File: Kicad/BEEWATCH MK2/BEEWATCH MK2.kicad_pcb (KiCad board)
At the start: 4 copper layers, 40.3 x 39.7 mm, 118 parts, among them J1 USB_C_Receptacle_USB2.0_16P, J3 Conn_02x06_Odd_Even, Q1 DMG6968U, Q2 DMG6968U, Q3 DMP1045U-7, Q4 DMG6968U, Q5 BSS138, Q6 BSS138, Q7 BSS138, Q8 DMP1045U-7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

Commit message: Deep optmization 80% completed
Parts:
- moved R45 53.0 mm to (142.9, 120.3), turned to -135 degrees
- moved R44 53.0 mm to (143.8, 121.1), turned to -135 degrees
- moved R46 50.4 mm to (143.7, 118.5), turned to 135 degrees
- moved Q9 47.3 mm to (140.2, 119.3), turned to -135 degrees
- moved R47 45.1 mm to (141.7, 116.5), turned to 135 degrees
- moved R33 42.1 mm to (160.1, 101.3), turned to -45 degrees
- moved C24 39.5 mm to (140.4, 114.6)
- moved Q7 37.0 mm to (158.2, 103.2), turned to -135 degrees
- moved C22 35.2 mm to (140.0, 107.4), turned to 180 degrees
- moved C23 35.0 mm to (140.1, 108.7), turned to 180 degrees
- moved U5 34.6 mm to (140.1, 111.5), turned to -90 degrees
- moved R43 33.0 mm to (138.0, 117.0), turned to 135 degrees
- moved R36 31.4 mm to (155.9, 104.7), turned to 135 degrees
- moved R48 30.1 mm to (140.7, 105.7), turned to -90 degrees
- moved C30 28.9 mm to (137.5, 113.9), turned to 90 degrees
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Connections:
- Q3 pad 1: VBUS -> /Battery&BMS/VBAT
- Q3 pad 2: +VBAT -> VBUS
- Q3 pad 3: /Battery&BMS/VBAT -> +VBAT
- R44 pad 1: +VBAT -> /Battery&BMS/+VBAT_IN
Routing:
- net Net-(Q4-D): track 0.00 -> 4.43 mm
- net +3.3V: track 0.00 -> 1.78 mm
- net /ESP32/GPS_EN: track 0.00 -> 1.74 mm

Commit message: Deep optmization 90% completed
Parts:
- J3: footprint Connector_PinHeader_1.27mm:PinHeader_2x06_P1.27mm_Vertical -> Connector_PinHeader_1.27mm:PinHeader_2x06_P1.27mm_Vertical_SMD
- TP1: moved to F.Cu
- moved BT1 37.7 mm to (141.1, 105.2)
- moved TP1 13.2 mm to (158.7, 108.9)
- moved C18 4.23 mm to (151.3, 116.1)
- moved R19 3.59 mm to (155.1, 121.6), turned to 90 degrees
- moved R53 3.54 mm to (154.6, 93.9)
- moved J3 3.35 mm to (150.0, 121.3)
- moved R4 3.28 mm to (146.9, 107.5)
- moved Q2 3.02 mm to (159.3, 119.4)
- moved R18 3.01 mm to (159.4, 116.8)
- moved R17 3.01 mm to (155.9, 118.4)
- moved R6 2.36 mm to (168.5, 106.4), turned to 0 degrees
- moved C21 1.68 mm to (142.8, 103.2)
- moved C13 1.60 mm to (159.4, 111.6), turned to -135 degrees
- moved R25 1.50 mm to (133.5, 97.3)
- moved R34 1.50 mm to (145.6, 117.0)
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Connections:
- net Net-(C28-Pad1) renamed /RYS8830/+0.92V
- net Net-(U2-SW) renamed /RYS8830/SW
- net Net-(U2-VFB) renamed /RYS8830/FB
- C10 pad 1: 3V3 -> +3.3V
- C11 pad 1: 3V3 -> +3.3V
- C5 pad 1: 3V3 -> +3.3V
- C6 pad 1: 3V3 -> +3.3V
- C7 pad 1: 3V3 -> +3.3V
- C8 pad 1: 3V3 -> +3.3V
- D1 pad 1: 3V3 -> +3.3V
- L1 pad 2: 3V3 -> +3.3V
- R3 pad 2: 3V3 -> +3.3V
- R5 pad 2: 3V3 -> +3.3V
- R6 pad 2: 3V3 -> +3.3V
- U1 pad 20: 3V3 -> +3.3V
- U1 pad 46: 3V3 -> +3.3V
- U1 pad 55: 3V3 -> +3.3V
- U1 pad 56: 3V3 -> +3.3V
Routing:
- net GND: track 0.00 -> 37.9 mm, vias 0 -> 32
- net /ACCELEROMETER/MPU_SCL: track 0.00 -> 20.5 mm, vias 0 -> 2
- net /ACCELEROMETER/MPU_SDA: track 0.00 -> 19.4 mm, vias 0 -> 2
- net +3.3V: track 1.78 -> 12.8 mm, vias 0 -> 1
- net /Battery&BMS/VBAT: track 0.00 -> 9.59 mm
- net /Battery&BMS/+VBAT_IN: track 0.00 -> 9.15 mm
- net /ESP32/XTAL_N: track 0.00 -> 8.72 mm
- net /RYS8830/GNSS_+1.8V: track 0.00 -> 8.16 mm
- net Net-(U1-CHIP_PU): track 0.00 -> 6.82 mm, vias 0 -> 2
- net /Battery&BMS/BAT_SENSE_EN: track 0.00 -> 6.51 mm
- net /RYS8830/FB: track 0.00 -> 6.39 mm
- net /ESP32/XTAL_P: track 0.00 -> 5.69 mm
- net /ESP32/XTAL_32K_P: track 0.00 -> 5.67 mm
- net /ESP32/XTAL_32K_N: track 0.00 -> 4.99 mm
- net /Battery&BMS/+3V3_IN: track 0.00 -> 4.64 mm
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- added copper zone on F.Cu, net +3.3V
- added copper zone on F.Cu, net /RYS8830/+0.92V
- added copper zone on F.Cu, net /RYS8830/SW
- added copper zone on F.Cu, net VDD3P3_RTC
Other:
- board text added: "ADD ANTENNA POLARITY IN SILK"

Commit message: Deep optimization 100%
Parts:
- added REF**: SMA_Amphenol_132289_EdgeMount, Connector_Coaxial:SMA_Amphenol_132289_EdgeMount, F.Cu at (166.6, 105.0)
- moved C10 12.0 mm to (148.6, 105.9), turned to 45 degrees
- moved R53 8.70 mm to (145.9, 94.0)
- moved R17 1.04 mm to (155.6, 119.4)
- moved C26 0.72 mm to (142.4, 94.2), turned to 90 degrees
- moved L2 0.52 mm to (160.7, 113.7)
- moved R30 0.51 mm to (149.0, 104.0)
- moved R29 0.51 mm to (148.1, 103.3)
- moved R23 0.50 mm to (154.7, 115.1)
- moved C17 0.36 mm to (162.6, 91.2)
- moved TP1 0.36 mm to (159.0, 109.1)
- moved C15 0.36 mm to (159.4, 91.3)
- moved R7 0.30 mm to (144.5, 108.5)
- moved C13 0.28 mm to (159.6, 111.8)
- moved R16 0.28 mm to (164.6, 92.5)
- moved R8 0.22 mm to (143.8, 109.3)
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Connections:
- R34 pad 2: +3V3 -> +3.3V
- R35 pad 2: +3V3 -> +3.3V
- R36 pad 2: +3V3 -> +3.3V
- R37 pad 1: +3V3 -> +3.3V
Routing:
- net /RYS8830/GNSS_+1.8V: track 8.16 -> 49.9 mm
- net /RYS8830/TXD: track 0.00 -> 37.4 mm, vias 0 -> 2
- net /RYS8830/RXD: track 0.00 -> 36.6 mm, vias 0 -> 2
- net /Battery&BMS/CHG_ST: track 0.00 -> 27.3 mm, vias 0 -> 2
- net GND: track 37.9 -> 56.7 mm, vias 32 -> 48
- net +3.3V: track 12.8 -> 27.3 mm, vias 1 -> 14
- net Net-(Q7-S): track 1.85 -> 13.8 mm
- net Net-(U1-GPIO46): track 0.00 -> 11.8 mm, vias 0 -> 2
- net Net-(U1-GPIO45): track 0.00 -> 11.3 mm, vias 0 -> 2
- net /RYS8830/PPS: track 0.00 -> 10.8 mm, vias 0 -> 2
- net /RYS8830/+0.92V: track 0.00 -> 10.0 mm
- net Net-(U7-RTC_CLK_IN): track 0.00 -> 8.91 mm, vias 0 -> 2
- net Net-(Q6-D): track 1.35 -> 10.1 mm, vias 0 -> 2
- net /ESP32/GPS_TXD: track 0.00 -> 8.38 mm, vias 0 -> 2
- net Net-(U7-P06/BOOT_REC): track 0.00 -> 7.05 mm, vias 0 -> 2
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- added copper zone on B.Cu, net GND
- added copper zone on F.Cu, net GND
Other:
- board text added: "JLCJLCJLC"

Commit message: Routing ongoing
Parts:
- moved C18 7.48 mm to (156.4, 121.6), turned to -90 degrees
- moved R41 3.34 mm to (138.6, 99.8)
- moved Q3 0.46 mm to (141.6, 100.6)
- moved C21 0.30 mm to (142.8, 103.5)
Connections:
- U1 pad 40: /ESP32/BUZZER_EN -> unconnected-(U1-GPIO35-Pad40)
- U1 pad 7: /Battery&BMS/CHG_ST -> /ESP32/BUZZER_EN
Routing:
- net /Display/TFT_D/C: track 0.00 -> 32.9 mm, vias 0 -> 1
- net +1V8: track 5.07 -> 31.2 mm, vias 0 -> 2
- net /ESP32/IO1: track 0.00 -> 23.5 mm
- net /RYS8830/GNSS_+1.8V: track 49.9 -> 72.9 mm, vias 0 -> 4
- net /Display/TFT_CS: track 0.00 -> 22.7 mm, vias 0 -> 1
- net GND: track 56.7 -> 79.4 mm, vias 48 -> 70
- net /ESP32/BAT_VSENSE: track 1.67 -> 23.2 mm, vias 0 -> 2
- net Net-(BZ1--): track 0.00 -> 19.2 mm
- net /Display/TFT_LED_PIN: track 0.00 -> 18.0 mm, vias 0 -> 1
- net VBUS: track 8.64 -> 25.7 mm, vias 0 -> 3
- net +3.3V: track 27.3 -> 43.5 mm, vias 14 -> 23
- net /ESP32/D+: track 0.00 -> 15.2 mm, vias 0 -> 3
- net /Battery&BMS/+VBAT_IN: track 9.15 -> 23.5 mm, vias 0 -> 2
- net /ESP32/D-: track 0.00 -> 13.0 mm, vias 0 -> 1
- net GNSS_+1V8: track 0.00 -> 12.2 mm
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
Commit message: Layout ongoing
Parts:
- R29, R30: moved to B.Cu
- moved C18 13.0 mm to (143.4, 121.7), turned to 90 degrees
- moved R17 10.8 mm to (144.8, 119.0), turned to -90 degrees
- moved R19 10.4 mm to (144.7, 121.7), turned to -90 degrees
- moved R30 10.1 mm to (153.4, 94.9), turned to 180 degrees
- moved R29 8.61 mm to (146.2, 94.9), turned to 0 degrees
- moved R18 3.22 mm to (156.8, 118.8)
- moved Q2 3.22 mm to (156.8, 121.4)
- moved R52 1.71 mm to (159.9, 117.3)
- moved C1 1.63 mm to (155.4, 117.0)
- moved Y1 1.63 mm to (156.9, 115.7)
- moved C2 1.58 mm to (158.3, 114.4)
- moved R51 1.48 mm to (159.1, 118.1)
- moved R23 1.06 mm to (155.5, 114.4)
- moved R53 0.90 mm to (145.5, 93.2)
- moved C5 0.72 mm to (156.3, 112.8)
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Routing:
- net /ESP32/IO0: track 8.94 -> 39.9 mm, vias 0 -> 5
- net /Display/TFT_RST: track 0.00 -> 28.5 mm, vias 0 -> 3
- net /RYS8830/GNSS_+1.8V: track 72.9 -> 97.6 mm, vias 4 -> 6
- net /ESP32/BUZZER_EN: track 0.00 -> 17.1 mm, vias 0 -> 1
- net /ESP32/IO1: track 23.5 -> 40.3 mm, vias 0 -> 3
- net /Display/TFT_D/C: track 32.9 -> 16.8 mm
- net /Display/TFT_SDI: track 0.00 -> 15.4 mm, vias 0 -> 3
- net /Display/TFT_SCK: track 0.00 -> 13.2 mm, vias 0 -> 1
- net /ACCELEROMETER/MPU_INT: track 6.89 -> 18.5 mm, vias 1 -> 2
- net /ESP32/BAT_VSENSE: track 23.2 -> 12.0 mm
- net Net-(U1-GPIO45): track 8.35 -> 0.00 mm, vias 2 -> 0
- net Net-(U1-GPIO46): track 7.65 -> 0.00 mm, vias 2 -> 0
- net /RYS8830/RXD: track 45.5 -> 38.6 mm
- net /Display/TFT_CS: track 22.7 -> 15.9 mm
- net Net-(U7-RTC_CLK_IN): track 8.91 -> 2.43 mm, vias 2 -> 1
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- removed copper zone on F.Cu, net +3.3V
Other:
- outline, holes or cut-outs redrawn

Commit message: Layout almost completed
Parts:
- moved R4 3.74 mm to (144.8, 104.4)
- moved C10 1.60 mm to (148.5, 104.3), turned to 135 degrees
- moved C4 0.36 mm to (143.6, 105.5)
- moved C3 0.36 mm to (145.9, 103.2)
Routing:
- net /ESP32/GPS_EN: track 1.74 -> 13.6 mm, vias 0 -> 2
- net /ESP32/BAT_VSENSE: track 12.0 -> 22.2 mm
- net Net-(U1-GPIO46): track 0.00 -> 10.2 mm
- net Net-(U1-GPIO45): track 0.00 -> 9.80 mm
- net /ESP32/LED1: track 0.00 -> 9.50 mm, vias 0 -> 1
- net /ACCELEROMETER/MPU_INT: track 18.5 -> 25.8 mm
- net /ESP32/GPS_TXD: track 14.5 -> 8.44 mm
- net /Display/TFT_SDI: track 15.4 -> 19.7 mm
- net /Display/TFT_RST: track 28.5 -> 32.5 mm
- net /Display/TFT_CS: track 15.9 -> 18.5 mm
- net /ESP32/GPS_RXD: track 9.48 -> 7.38 mm
- net /Battery&BMS/CHG_ST: track 27.8 -> 25.8 mm
- net /ACCELEROMETER/MPU_SCL: track 20.9 -> 18.9 mm, vias 2 -> 1
- net /ESP32/IO0: track 39.9 -> 38.3 mm
- net /ESP32/XTAL_32K_N: track 4.80 -> 6.02 mm
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
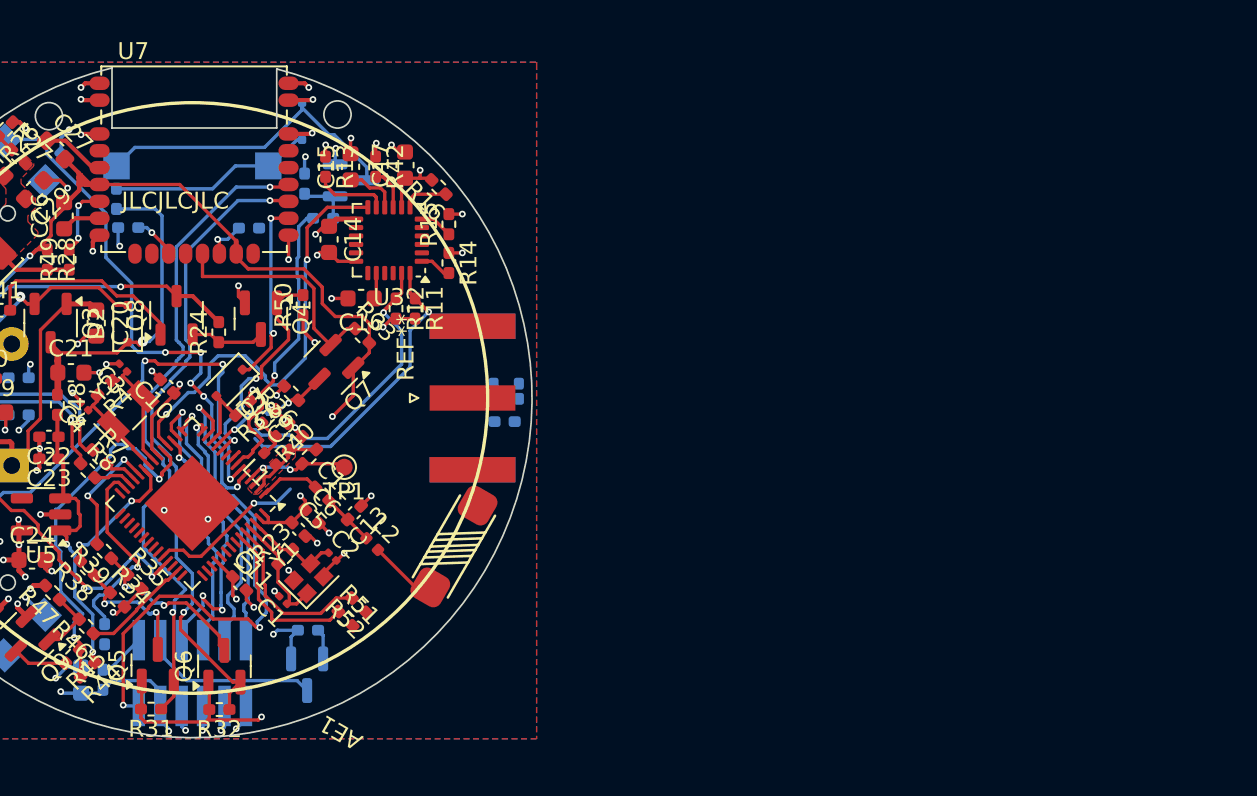
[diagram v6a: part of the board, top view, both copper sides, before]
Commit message: Somehow finished the layout, but deep optimization required
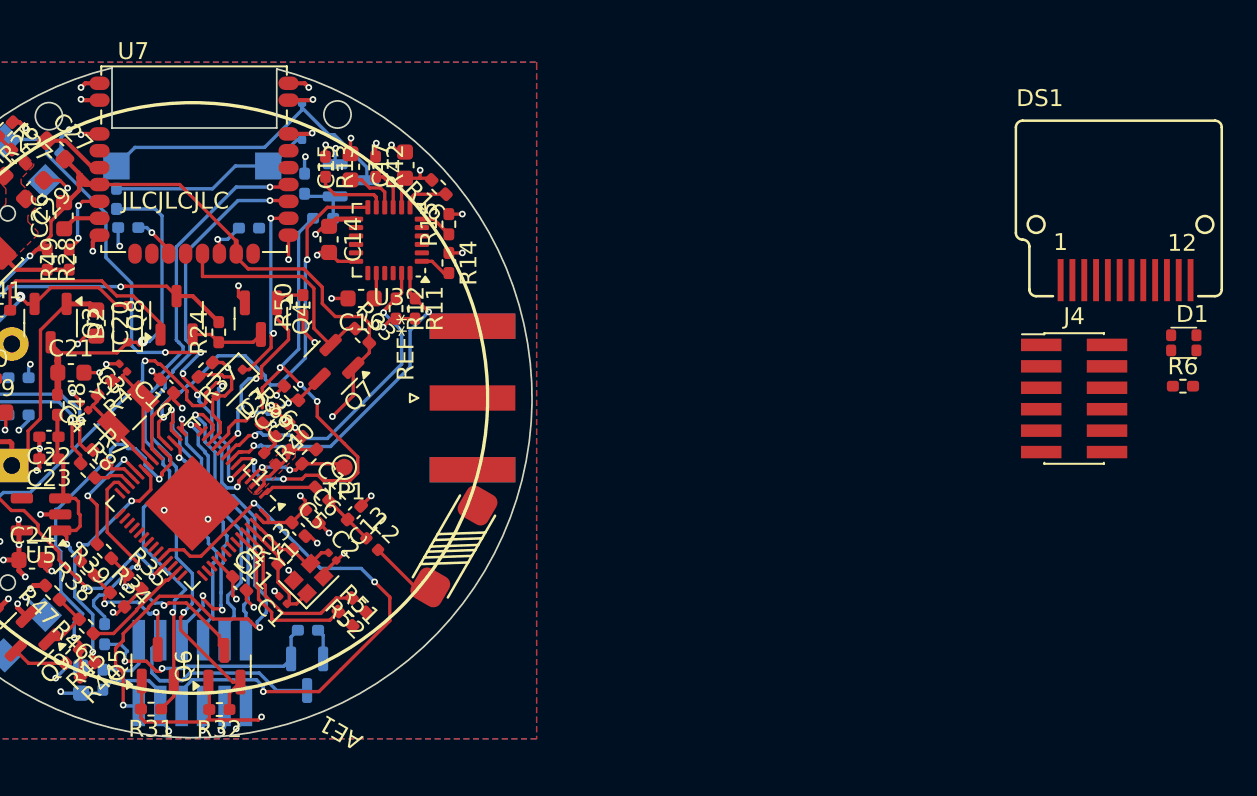
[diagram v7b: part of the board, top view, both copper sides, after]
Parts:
- added DS1: GC9A01, DISPLAY:GC9A01_BOTTOM, F.Cu at (205.3, 92.3)
- added J4: Conn_02x06_Odd_Even, Connector_PinHeader_1.27mm:PinHeader_2x06_P1.27mm_Vertical_SMD, F.Cu at (202.3, 105.0)
- D1, R6: moved to F.Cu
- moved D1 40.3 mm to (208.8, 101.7)
- moved R6 40.3 mm to (208.7, 104.3)
- moved R37 3.18 mm to (150.8, 103.3)
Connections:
- D1 pad 1: +3.3V -> /Display board/3V3
- D1 pad 2: /ESP32/LED1 -> /Display board/_LED
- D1 pad 3: GND -> /Display board/_GND
- J3 pad 6: GND -> /Display/LED
- R6 pad 1: /ESP32/LED1 -> /Display board/_LED
- R6 pad 2: +3.3V -> /Display board/3V3
- U1 pad 38: /ESP32/LED1 -> /Display/LED
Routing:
- net /Display/LED: track 0.00 -> 34.5 mm, vias 0 -> 3
- net /ESP32/BUZZER_EN: track 17.8 -> 29.4 mm, vias 1 -> 5
- net Net-(Q2-G): track 3.44 -> 14.5 mm, vias 1 -> 2
- net /ESP32/LED1: track 9.50 -> 0.00 mm, vias 1 -> 0
- net /ESP32/GPS_PSS: track 4.68 -> 7.02 mm
- net /Display/TFT_LEDK: track 10.4 -> 12.7 mm
- net /ACCELEROMETER/MPU_SCL: track 18.9 -> 20.7 mm, vias 1 -> 2
- net GND: track 77.8 -> 76.3 mm, vias 62 -> 61
- net +3.3V: track 46.8 -> 48.1 mm
- net /ESP32/IO1: track 39.5 -> 40.6 mm
- net /ACCELEROMETER/MPU_SDA: track 18.5 -> 19.5 mm, vias 1 -> 2
- net /Display/TFT_LEDA: track 2.85 -> 3.72 mm
- net /Display/TFT_CS: track 18.5 -> 17.7 mm
- net /ESP32/GPS_EN: track 13.6 -> 12.9 mm

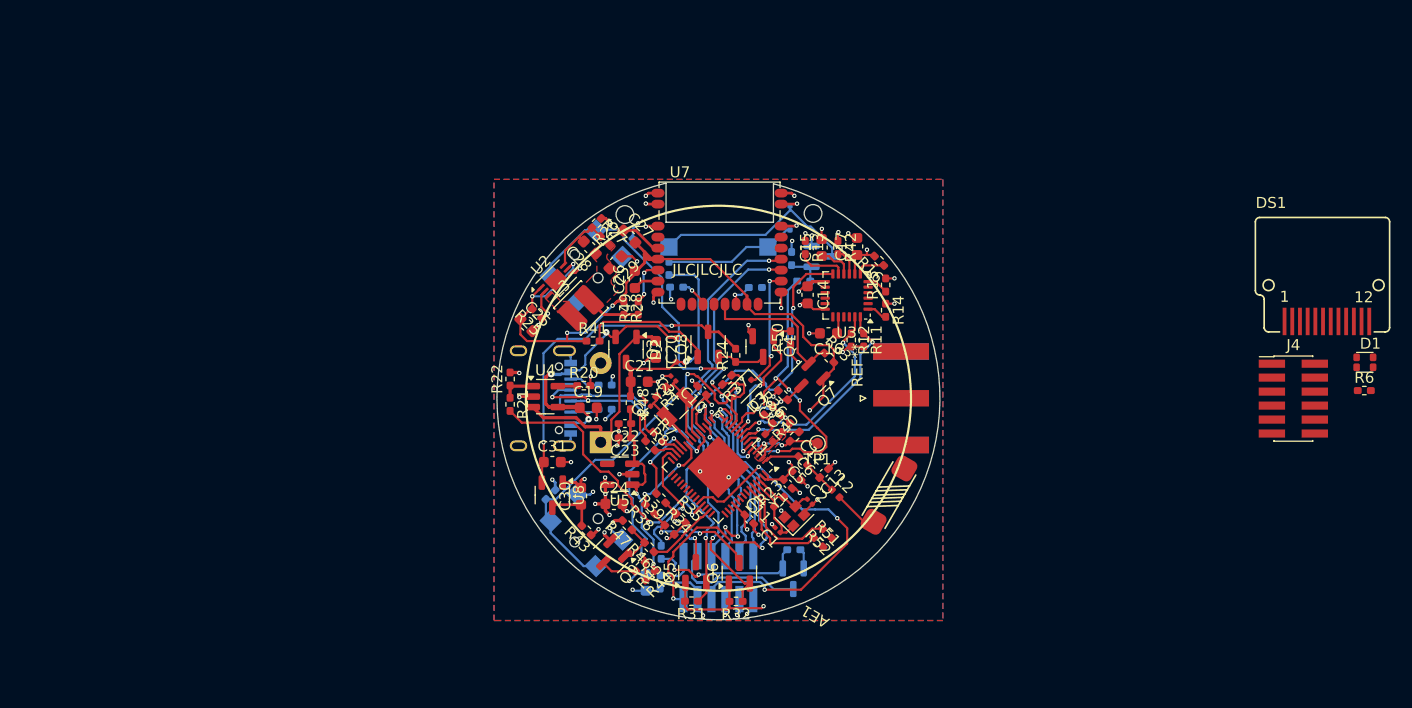
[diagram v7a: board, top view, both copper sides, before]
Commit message: Layout Finished but deep otimization required
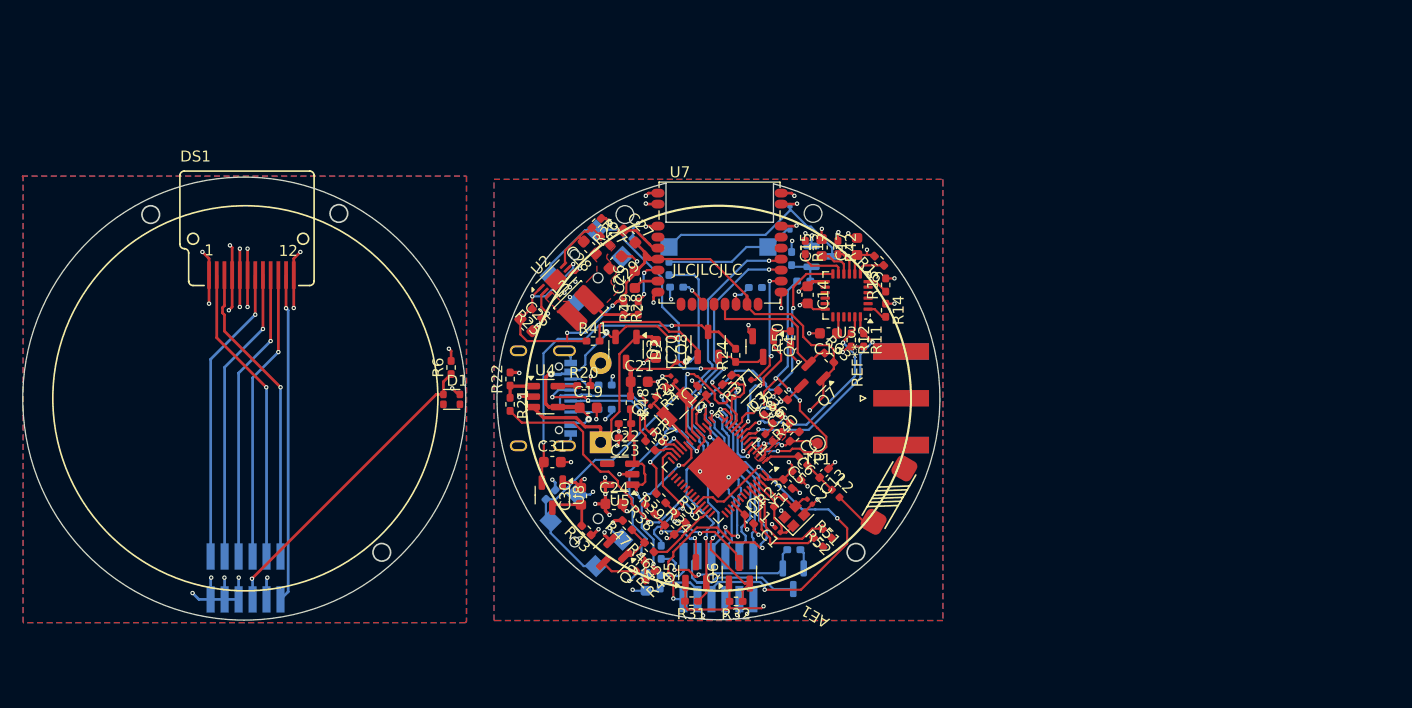
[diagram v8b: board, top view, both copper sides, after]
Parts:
- J4: moved to B.Cu
- moved DS1 97.8 mm to (107.5, 88.1)
- moved J4 96.6 mm to (107.0, 121.3), turned to -90 degrees
- moved D1 83.1 mm to (125.8, 105.1)
- moved R6 83.0 mm to (125.7, 102.2), turned to 90 degrees
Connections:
- J4 pad 1: /Display board/LED_A -> /Display board/D/C
- J4 pad 10: /Display board/_GND -> /Display board/3V3
- J4 pad 11: /Display board/D/C -> /Display board/LED_A
- J4 pad 12: /Display board/_GND -> /Display board/RST
- J4 pad 2: /Display board/RST -> /Display board/_GND
- J4 pad 3: /Display board/LED_K -> /Display board/CS
- J4 pad 4: /Display board/3V3 -> /Display board/_GND
- J4 pad 5: /Display board/SDI -> /Display board/SCK
- J4 pad 6: /Display board/_LED -> /Display board/_GND
- J4 pad 7: /Display board/SCK -> /Display board/SDI
- J4 pad 8: /Display board/_GND -> /Display board/_LED
- J4 pad 9: /Display board/CS -> /Display board/LED_K
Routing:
- net /Display board/_GND: track 0.00 -> 31.3 mm, vias 0 -> 12
- net /Display board/RST: track 0.00 -> 29.8 mm, vias 0 -> 1
- net /Display board/_LED: track 0.00 -> 28.4 mm, vias 0 -> 1
- net /Display board/LED_A: track 0.00 -> 27.8 mm, vias 0 -> 1
- net /Display board/LED_K: track 0.00 -> 27.5 mm, vias 0 -> 1
- net /Display board/D/C: track 0.00 -> 27.3 mm, vias 0 -> 1
- net /Display board/CS: track 0.00 -> 27.0 mm, vias 0 -> 1
- net /Display board/SCK: track 0.00 -> 26.8 mm, vias 0 -> 1
- net /Display board/SDI: track 0.00 -> 26.6 mm, vias 0 -> 1
- net /Display board/3V3: track 0.00 -> 10.2 mm, vias 0 -> 5
- net GND: vias 61 -> 65
- added copper zone on In2.Cu, net /Display board/3V3
- added copper zone on B.Cu, net /Display board/_GND
- added copper zone on F.Cu, net /Display board/_GND
- added copper zone on In1.Cu, net /Display board/_GND
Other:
- board size 40.3 x 39.7 mm -> 83.4 x 40.3 mm
